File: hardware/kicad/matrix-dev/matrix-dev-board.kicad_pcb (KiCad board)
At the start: 2 copper layers, 22.9 x 24.1 mm, 21 parts, among them J1 CONN_01X01, J2 CONN_01X04, J3 CONN_01X16, J4 CONN_01X12, J5 Screw_Terminal_1x02, U1 IS31FL3733

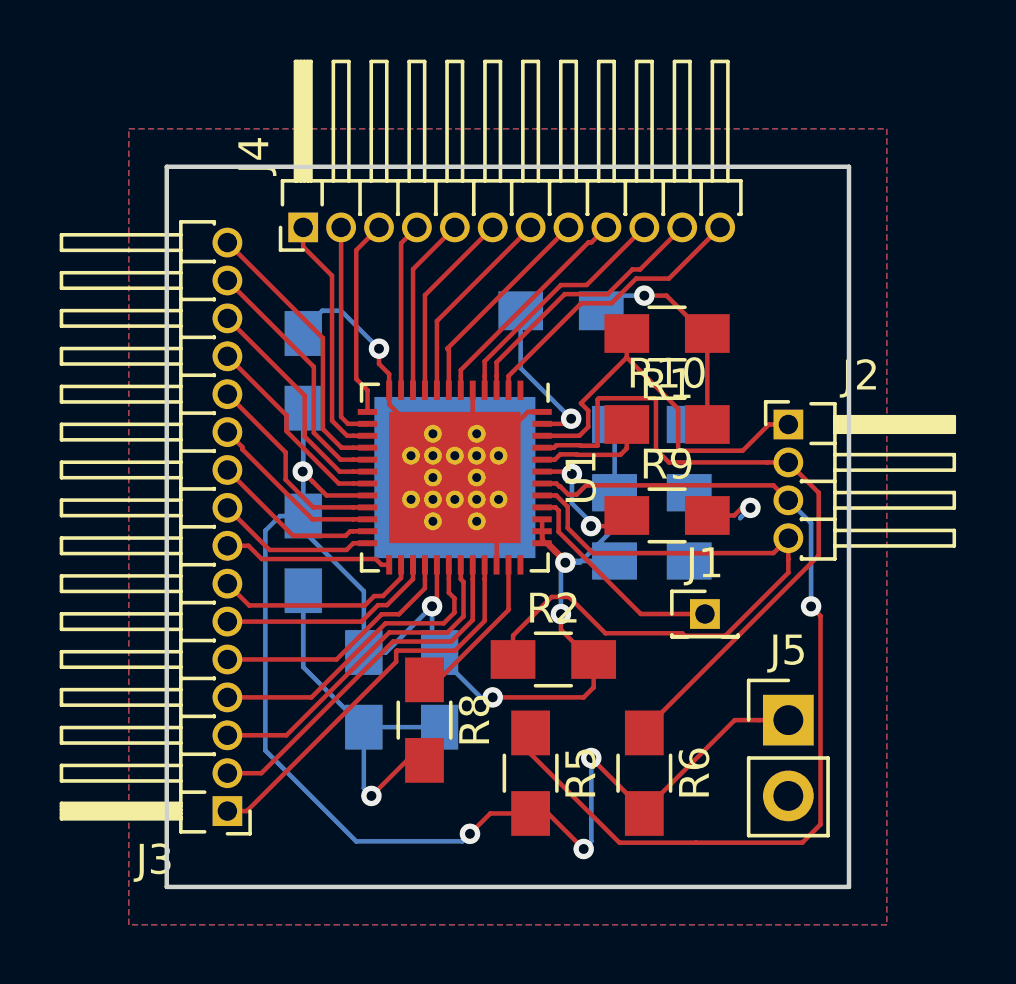
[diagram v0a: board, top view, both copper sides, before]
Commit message: [ci skip] Clean up silk layer and add extra labels
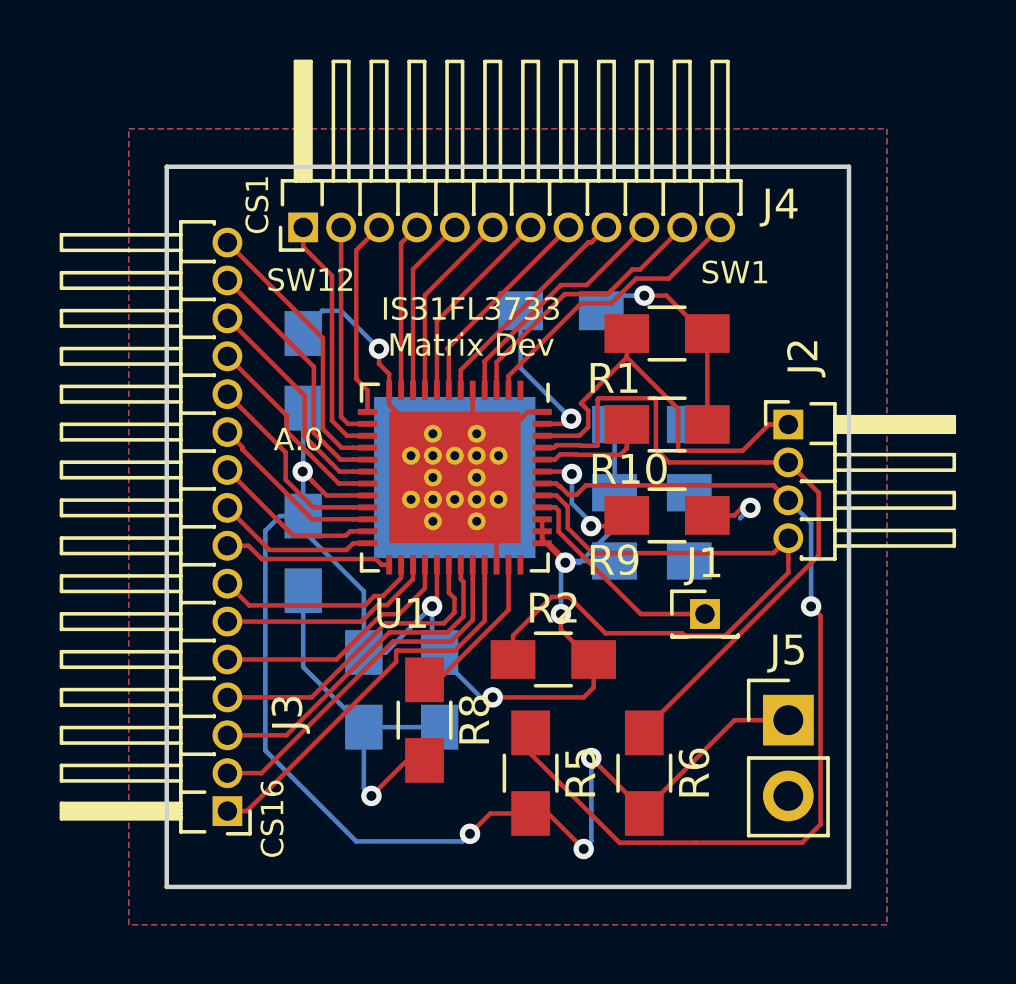
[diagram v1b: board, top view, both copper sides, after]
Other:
- board text added: "A.0"
- board text added: "CS1"
- board text added: "CS16"
- board text added: "IS31FL3733 Matrix Dev"
- board text added: "Rev A.0"
- board text added: "SW1"
- board text added: "SW12"
- board text added: "Stephen Legge"
- board text added: "[ A Legge Up ]"
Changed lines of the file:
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@@
     (area 133.274999 110.414999 156.285001 134.695001)
     (thickness 1.6)
-    (drawings 4)
+    (drawings 13)
     (tracks 347)
     (zones 0)
@@
     (46 B.CrtYd user)
     (47 F.CrtYd user)
-    (48 B.Fab user hide)
-    (49 F.Fab user hide)
+    (48 B.Fab user)
+    (49 F.Fab user)
   )
   (setup
@@
     (pad_to_mask_clearance 0.0508)
     (aux_axis_origin 0 0)
-    (visible_elements FFFEFFFF)
+    (visible_elements 7FFFFFFF)
     (pcbplotparams
       (layerselection 0x00030_80000001)
@@
     (tags "QFN 0.4")
     (attr smd)
-    (fp_text reference U1 (at 0 -4.25 270) (layer F.SilkS)
+    (fp_text reference U1 (at 4.572 1.778 360) (layer F.SilkS)
       (effects (font (size 1 1) (thickness 0.15)))
     )
@@
     (tags "capacitor 0805")
     (attr smd)
-    (fp_text reference C1 (at 0 1.75) (layer B.SilkS)
+    (fp_text reference C1 (at 3.014 0.034) (layer B.SilkS)
       (effects (font (size 1 1) (thickness 0.15)) (justify mirror))
     )
@@
     (tags "capacitor 0805")
     (attr smd)
-    (fp_text reference C4 (at -3.1115 -1.016 90) (layer B.SilkS)
+    (fp_text reference C4 (at -3.084 0.026 90) (layer B.SilkS)
       (effects (font (size 1 1) (thickness 0.15)) (justify mirror))
     )
@@
     (tags "capacitor 0805")
     (attr smd)
-    (fp_text reference C5 (at -3.048 -1.3335 90) (layer B.SilkS)
+    (fp_text reference C5 (at -3.094 -0.024 90) (layer B.SilkS)
       (effects (font (size 1 1) (thickness 0.15)) (justify mirror))
     )
@@
     (tags "capacitor 0805")
     (attr smd)
-    (fp_text reference C6 (at 0 1.75 180) (layer B.SilkS)
+    (fp_text reference C6 (at -3.074 -0.078 180) (layer B.SilkS)
       (effects (font (size 1 1) (thickness 0.15)) (justify mirror))
     )
@@
     (tags "capacitor 0805")
     (attr smd)
-    (fp_text reference C7 (at 0 1.75 180) (layer B.SilkS)
+    (fp_text reference C7 (at -3.054 -0.032 180) (layer B.SilkS)
       (effects (font (size 1 1) (thickness 0.15)) (justify mirror))
     )
@@
     (descr "Through hole angled pin header, 1x04, 1.27mm pitch, 4.0mm pin length, single row")
     (tags "Through hole angled pin header THT 1x04 1.27mm single row")
-    (fp_text reference J2 (at 2.4325 -1.635) (layer F.SilkS)
+    (fp_text reference J2 (at 0.508 -2.286 90) (layer F.SilkS)
       (effects (font (size 1 1) (thickness 0.15)))
     )
@@
     (descr "Through hole angled pin header, 1x16, 1.27mm pitch, 4.0mm pin length, single row")
     (tags "Through hole angled pin header THT 1x16 1.27mm single row")
-    (fp_text reference J3 (at 2.4325 -1.635 180) (layer F.SilkS)
+    (fp_text reference J3 (at -2.032 3.302 270) (layer F.SilkS)
       (effects (font (size 1 1) (thickness 0.15)))
     )
@@
     (descr "Through hole angled pin header, 1x12, 1.27mm pitch, 4.0mm pin length, single row")
     (tags "Through hole angled pin header THT 1x12 1.27mm single row")
-    (fp_text reference J4 (at 2.4325 -1.635 90) (layer F.SilkS)
+    (fp_text reference J4 (at 0.762 16.002 180) (layer F.SilkS)
       (effects (font (size 1 1) (thickness 0.15)))
     )
@@
     (tags "resistor 0805")
     (attr smd)
-    (fp_text reference R1 (at 0 -1.7 180) (layer F.SilkS)
+    (fp_text reference R1 (at 1.778 -1.524 180) (layer F.SilkS)
       (effects (font (size 1 1) (thickness 0.15)))
     )
@@
     (tags "resistor 0805")
     (attr smd)
-    (fp_text reference R9 (at 0 -1.7) (layer F.SilkS)
+    (fp_text reference R9 (at -1.778 1.524) (layer F.SilkS)
       (effects (font (size 1 1) (thickness 0.15)))
     )
@@
     (tags "resistor 0805")
     (attr smd)
-    (fp_text reference R10 (at 0 -1.7) (layer F.SilkS)
+    (fp_text reference R10 (at -1.27 1.524) (layer F.SilkS)
       (effects (font (size 1 1) (thickness 0.15)))
     )
@@
       (rotate (xyz 0 0 -90))
     )
+  )
+  (gr_text "[ A Legge Up ]" (at 148.56 130.42) (layer B.SilkS)
+    (effects (font (size 0.75 0.75) (thickness 0.1875)) (justify mirror))
+  )
+  (gr_text A.0 (at 137.77 119.64) (layer F.SilkS)
+    (effects (font (size 0.75 0.75) (thickness 0.1875)))
+  )
+  (gr_text "IS31FL3733\nMatrix Dev" (at 143.55 115.87) (layer F.SilkS)
+    (effects (font (size 0.75 0.75) (thickness 0.1875)))
+  )
+  (gr_text "Stephen Legge" (at 148.81 129.05) (layer B.SilkS)
+    (effects (font (size 0.75 0.75) (thickness 0.1875)) (justify mirror))
+  )
+  (gr_text "Rev A.0" (at 148.97 127.28) (layer B.SilkS)
+    (effects (font (size 1.5 1.5) (thickness 0.3)) (justify mirror))
+  )
+  (gr_text SW1 (at 152.4 114.046) (layer F.SilkS)
+    (effects (font (size 0.75 0.75) (thickness 0.1875)))
+  )
+  (gr_text SW12 (at 138.176 114.3) (layer F.SilkS)
+    (effects (font (size 0.75 0.75) (thickness 0.1875)))
+  )
+  (gr_text CS1 (at 136.398 111.76 90) (layer F.SilkS)
+    (effects (font (size 0.75 0.75) (thickness 0.1875)))
+  )
+  (gr_text CS16 (at 136.906 132.334 90) (layer F.SilkS)
+    (effects (font (size 0.75 0.75) (thickness 0.1875)))
   )
   (gr_line (start 133.35 134.62) (end 133.35 110.49) (angle 90) (layer Edge.Cuts) (width 0.15))
@@
       )
     )
+  )
+  (zone (net 0) (net_name "") (layer B.SilkS) (hatch none 0.508)
+    (connect_pads (clearance 0.508))
+    (min_thickness 0.254)
+    (fill yes (arc_segments 16) (thermal_gap 0.508) (thermal_bridge_width 0.508))
+    (polygon
+      (pts
+        (xy 141.495 116.125) (xy 143.835 119.365) (xy 146.725 119.365) (xy 142.745 114.675)
+      )
+    )
+  )
+  (zone (net 0) (net_name "") (layer B.SilkS) (hatch none 0.508)
+    (connect_pads (clearance 0.508))
+    (min_thickness 0.254)
+    (fill yes (arc_segments 16) (thermal_gap 0.508) (thermal_bridge_width 0.508))
+    (polygon
+      (pts
+        (xy 138.705 119.365) (xy 141.595 119.375) (xy 142.635 117.955) (xy 142.571481 117.887008) (xy 141.815 116.665)
+        (xy 141.584316 116.830324) (xy 141.215 116.435)
+      )
+    )

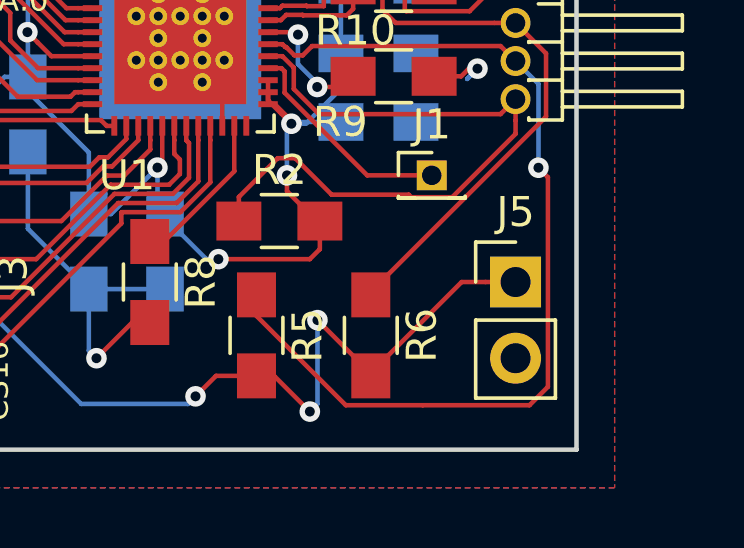
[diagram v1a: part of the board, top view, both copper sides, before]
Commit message: Add polarity indicators for power pins
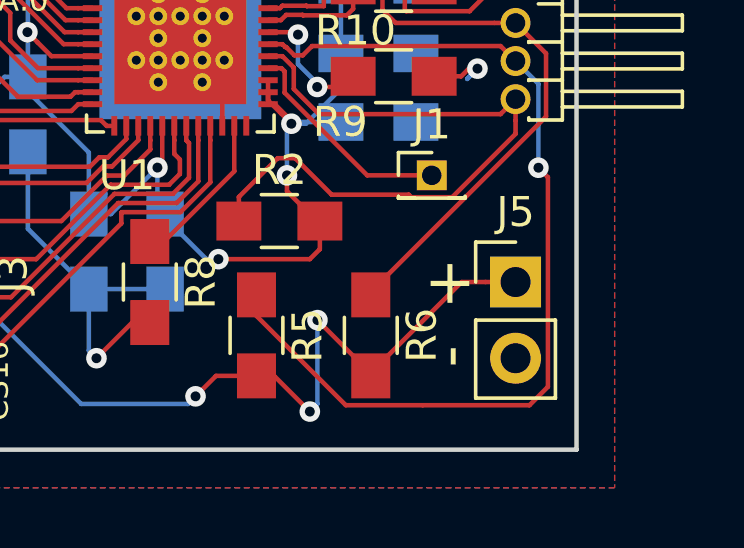
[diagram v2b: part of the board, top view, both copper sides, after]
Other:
- board text added: "+"
- board text added: "-"
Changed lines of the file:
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@@
     (area 133.274999 110.414999 156.285001 134.695001)
     (thickness 1.6)
-    (drawings 13)
+    (drawings 15)
     (tracks 347)
     (zones 0)
@@
     )
   )
+  (gr_text - (at 151.97 131.51 90) (layer F.SilkS)
+    (effects (font (size 1.5 1.5) (thickness 0.3)))
+  )
+  (gr_text + (at 151.99 129.03) (layer F.SilkS)
+    (effects (font (size 1.5 1.5) (thickness 0.3)))
+  )
   (gr_text "[ A Legge Up ]" (at 148.56 130.42) (layer B.SilkS)
